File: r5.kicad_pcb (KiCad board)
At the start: 2 copper layers, 94.4 x 92.2 mm, 80 parts, among them J1 Conn_01x04, SW1 SW_SPDT, SW2 SW_SPDT, SW3 SW_SPDT, SW4 SW_SPDT, U1 LMZ22005, U10 74368PW, U100 Pico, U2 74LS365, U20 DRV8871DDA, U3 GY-BNO08X, U30 DRV8871DDA, U4 PI22, U40 DRV8871DDA, U5 SDD1309, U50 DRV8871DDA, U6 3X3HEADER, U60 DRV8871DDA, U70 DRV8871DDA, U80 PCA9685PW, X1 Conn_01x02, X2 Conn_01x02, X20 Conn_01x06, X30 Conn_01x06, X40 Conn_01x06, X50 Conn_01x06, X60 Conn_01x06, X70 Conn_01x06, X81 4X3HEADER

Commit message: wip
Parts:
- C90: moved to F.Cu
- D91: footprint LED_SMD:LED_WS2812B_PLCC4_5.0x5.0mm_P3.2mm -> LED_SMD:LED_WS2812B-2020_PLCC4_2.0x2.0mm; moved to F.Cu
- moved SW1 15.7 mm to (109.7, 137.4), turned to 90 degrees
- moved C90 14.0 mm to (97.0, 144.9), turned to 0 degrees
- moved D91 10.1 mm to (93.2, 144.8), turned to 180 degrees

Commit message: wip
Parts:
- removed C1: 10u, Capacitor_SMD:C_1206_3216Metric_Pad1.33x1.80mm_HandSolder
- removed U10: 74368PW, Package_SO:TSSOP-16_4.4x5mm_P0.65mm
- added J2: Conn_01x02, Connector_JST:JST_PH_B2B-PH-K_1x02_P2.00mm_Vertical, B.Cu at (86.7, 68.1)
- added R18: 300R, Resistor_SMD:R_0805_2012Metric, F.Cu at (116.1, 116.4)
- added U7: 74HC540, Package_SO:TSSOP-20_4.4x6.5mm_P0.65mm, F.Cu at (105.4, 82.5)
- C10, C20, C30, C4, C40, C50, C60, C70, C90: footprint Capacitor_SMD:C_0805_2012Metric_Pad1.18x1.45mm_HandSolder -> Capacitor_SMD:C_0805_2012Metric
- C2: value 10u -> 22u; footprint Capacitor_SMD:C_1206_3216Metric_Pad1.33x1.80mm_HandSolder -> Capacitor_SMD:C_1206_3216Metric
- C21, C31, C41, C51, C61, C71: value CP -> 22u; footprint Capacitor_SMD:CP_Elec_5x5.7 -> Capacitor_SMD:C_1206_3216Metric
- C80: value 10u -> 100n; footprint Capacitor_SMD:C_0805_2012Metric_Pad1.18x1.45mm_HandSolder -> Capacitor_SMD:C_0805_2012Metric
- C81: value CP -> 220u; footprint Capacitor_THT:CP_Radial_D6.3mm_P2.50mm -> Capacitor_SMD:CP_Elec_6.3x7.7
- D90: value DIODE-SOD523 -> 1N4148; footprint Diode_SMD:D_SOD-523 -> Diode_SMD:D_SOD-323
- D91: footprint LED_SMD:LED_WS2812B-2020_PLCC4_2.0x2.0mm -> LED_SMD:LED_WS2812B_PLCC4_5.0x5.0mm_P3.2mm
- R1, R10, R11, R12, R13, R14, R15, R16, R17, R3, R7, R8, R9: footprint Resistor_SMD:R_0805_2012Metric_Pad1.20x1.40mm_HandSolder -> Resistor_SMD:R_0805_2012Metric
- R2: value 1k3 -> 1k; footprint Resistor_SMD:R_0805_2012Metric_Pad1.20x1.40mm_HandSolder -> Resistor_SMD:R_0805_2012Metric
- R20, R30, R4, R40, R50, R60, R70: value 33k -> 68k; footprint Resistor_SMD:R_0805_2012Metric_Pad1.20x1.40mm_HandSolder -> Resistor_SMD:R_0805_2012Metric
- R5, R6: value dnc -> ~; footprint Resistor_SMD:R_0805_2012Metric_Pad1.20x1.40mm_HandSolder -> Resistor_SMD:R_0805_2012Metric
- R90, R91: value 1k8 -> 4k7; footprint Resistor_SMD:R_0805_2012Metric_Pad1.20x1.40mm_HandSolder -> Resistor_SMD:R_0805_2012Metric
- U2: value 74LS365 -> 74HC365
- moved C90 88.2 mm to (104.8, 57.1), turned to 180 degrees
- moved D91 84.6 mm to (105.9, 61.1)
- moved X2 81.0 mm to (97.9, 144.8)
- moved R17 54.1 mm to (102.1, 70.5), turned to 90 degrees
- moved R16 50.2 mm to (99.8, 70.9), turned to 90 degrees
- moved R15 46.8 mm to (97.7, 70.8), turned to 90 degrees
- moved R90 40.4 mm to (70.6, 57.7)
- moved R91 36.3 mm to (68.8, 60.5), turned to 90 degrees
- moved X20 35.4 mm to (150.8, 83.6), turned to 180 degrees
- moved X70 33.7 mm to (150.8, 116.4), turned to 180 degrees
- moved R14 30.9 mm to (122.2, 81.9), turned to 90 degrees
- moved X30 23.0 mm to (150.8, 90.2), turned to 180 degrees
- moved X60 21.4 mm to (150.8, 109.8), turned to 180 degrees
- moved R10 15.9 mm to (118.4, 116.1)
- moved R3 12.9 mm to (119.4, 112.4)
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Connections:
- C21 pad 2: GND -> GNDPWR
- C31 pad 2: GND -> GNDPWR
- C41 pad 2: GND -> GNDPWR
- C51 pad 2: GND -> GNDPWR
- C61 pad 2: GND -> GNDPWR
- C71 pad 2: GND -> GNDPWR
- R2 pad 2: GND -> Net-(R18-Pad1)
- U20 pad 7: GND -> GNDPWR
- U30 pad 7: GND -> GNDPWR
- U40 pad 7: GND -> GNDPWR
- U50 pad 7: GND -> GNDPWR
- U60 pad 7: GND -> GNDPWR
- U70 pad 7: GND -> GNDPWR
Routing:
- net GND: track 11.7 -> 0.00 mm, vias 16 -> 0
- net +BATT: track 2.40 -> 0.00 mm
- net VBATMEASURE: track 2.00 -> 0.00 mm
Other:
- copper layers 2 -> 4

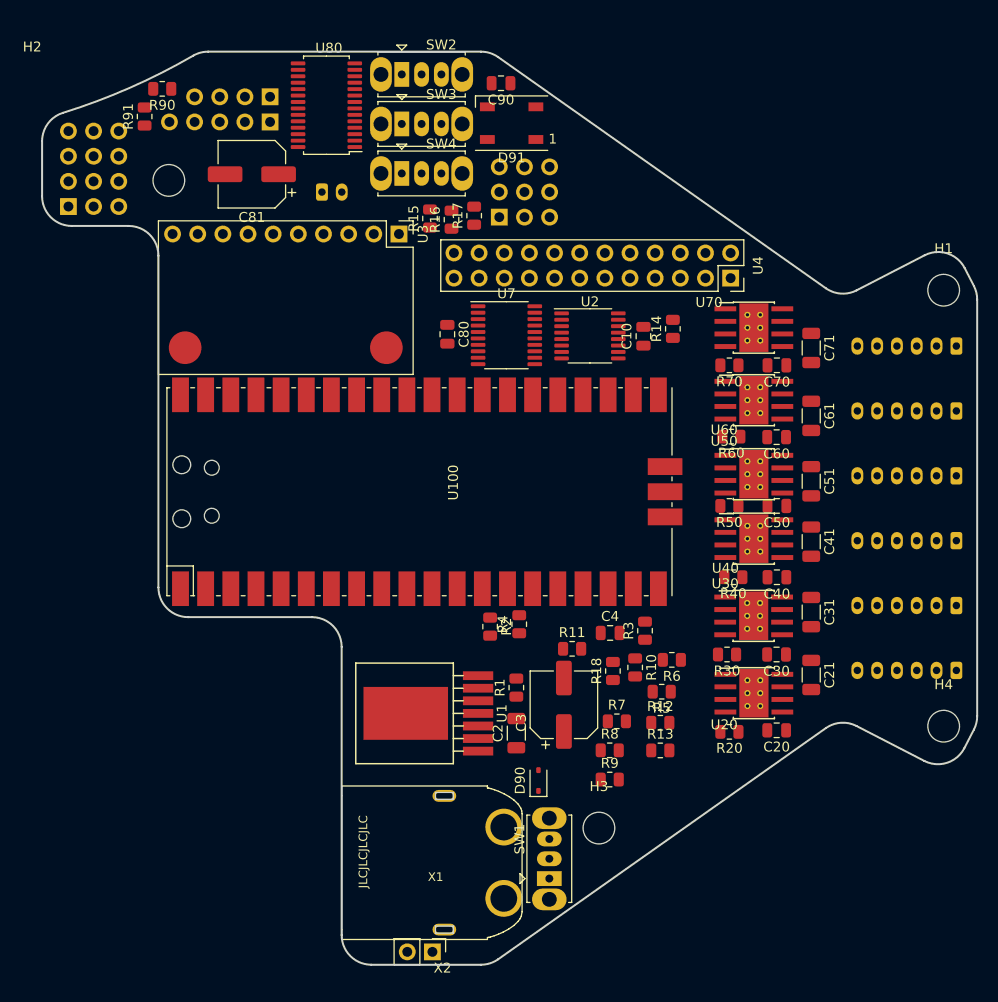
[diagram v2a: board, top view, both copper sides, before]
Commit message: component placement
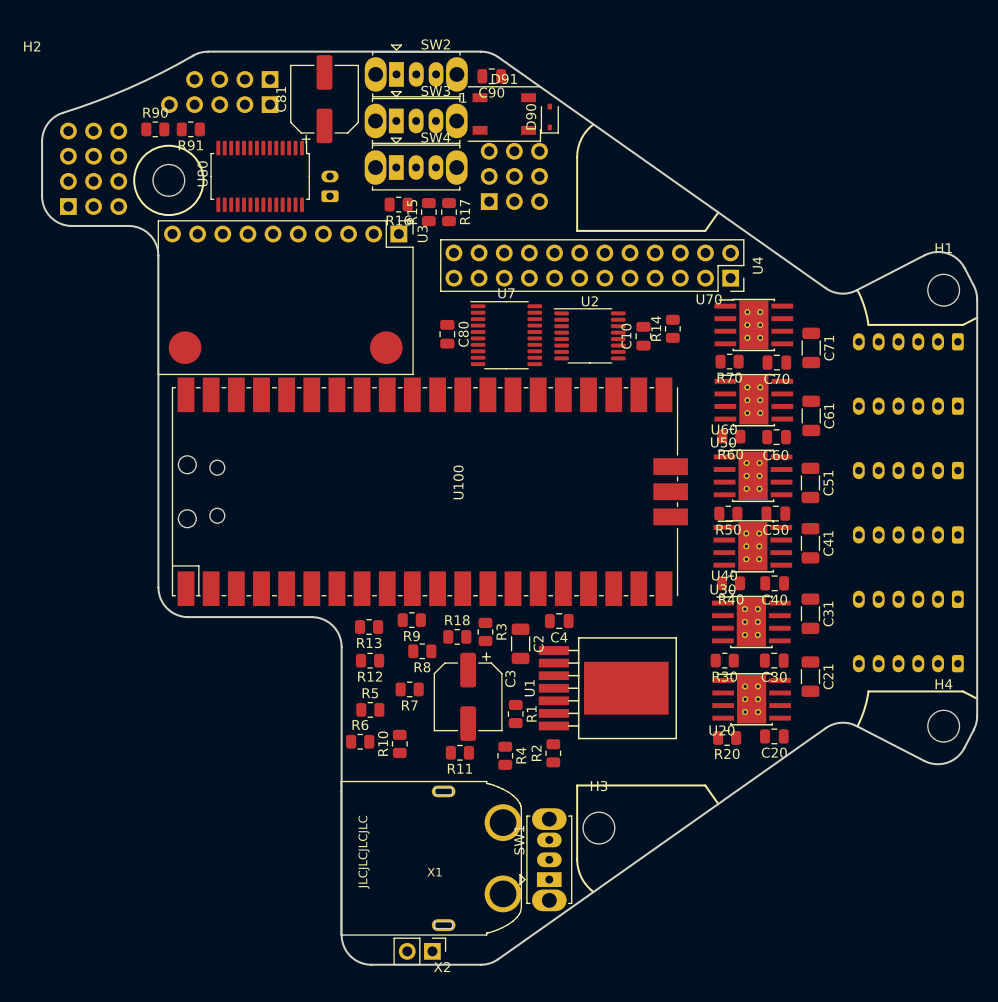
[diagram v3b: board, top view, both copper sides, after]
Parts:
- moved D90 67.0 mm to (109.8, 60.5)
- moved R6 32.5 mm to (90.6, 123.6), turned to 0 degrees
- moved R13 31.9 mm to (91.5, 112.0), turned to 180 degrees
- moved R12 30.0 mm to (91.6, 115.4), turned to 180 degrees
- moved R5 29.5 mm to (91.6, 120.4), turned to 0 degrees
- moved R9 25.7 mm to (95.8, 111.3), turned to 180 degrees
- moved R10 25.0 mm to (94.6, 123.8), turned to 90 degrees
- moved R8 21.4 mm to (96.9, 114.5), turned to 180 degrees
- moved R7 21.2 mm to (95.6, 118.3), turned to 180 degrees
- moved R3 16.1 mm to (103.2, 112.5), turned to -90 degrees
- moved R18 16.1 mm to (100.4, 113.0), turned to 0 degrees
- moved R11 15.4 mm to (100.7, 124.7), turned to 180 degrees
- moved R2 14.3 mm to (110.1, 124.8), turned to 90 degrees
- moved R4 13.4 mm to (105.2, 125.0), turned to -90 degrees
- moved C81 10.6 mm to (87.0, 58.7), turned to 90 degrees
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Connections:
- U100 pad 4: E6B -> E6A
- U100 pad 5: E6A -> E6B

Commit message: positions
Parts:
- removed the R17 at (99.6, 70.1)
- moved R40 55.2 mm to (70.8, 61.6), turned to 180 degrees
- moved R62 54.9 mm to (88.5, 68.7), turned to -90 degrees
- moved R61 51.6 mm to (90.5, 68.8), turned to -90 degrees
- moved R70 48.6 mm to (119.8, 82.2)
- moved R90 48.5 mm to (101.2, 70.1), turned to -90 degrees
- moved R92 48.3 mm to (111.2, 65.5), turned to -90 degrees
- moved R91 47.8 mm to (111.2, 68.9), turned to -90 degrees
- moved C28 38.0 mm to (132.5, 123.3)
- moved U25 38.0 mm to (130.1, 119.5)
- moved R25 38.0 mm to (127.7, 123.2), turned to 0 degrees
- moved C20 37.9 mm to (132.8, 85.2)
- moved R20 37.9 mm to (128.0, 85.3), turned to 0 degrees
- moved U20 37.9 mm to (130.5, 81.4)
- moved C23 33.5 mm to (137.0, 83.5)
- moved C31 32.4 mm to (137.1, 116.2)
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- renumbered C2 to C10, C3 to C11, C30 to C21, C40 to C22, C21 to C23, C31 to C24, C41 to C25, C50 to C26, C60 to C27, C70 to C28, C51 to C29, C61 to C30, C71 to C31, C90 to C40, C80 to C60, C4 to C70, C10 to C71, C81 to C90, D90 to D40, D91 to D41, H1 to H201, H2 to H202, H3 to H203, H4 to H204, R11 to R10, R12 to R11, R13 to R12, R1 to R13, R2 to R14, R18 to R15, R3 to R16, R4 to R17, R30 to R21, R40 to R22, R50 to R23, R60 to R24, R70 to R25, R14 to R40, R15 to R60, R5 to R61, R6 to R62, R10 to R70, R16 to R80, R7 to R90, R8 to R91, R9 to R92, R90 to R93, R91 to R94, SW1 to SW10, SW4 to SW60, SW2 to SW70, SW3 to SW80, U1 to U10, U30 to U21, U40 to U22, U50 to U23, U60 to U24, U70 to U25, U4 to U50, U80 to U60, U2 to U70, U7 to U71, U100 to U80, X1 to X10, X2 to X11, J2 to X12, X30 to X21, X40 to X22, X50 to X23, X60 to X24, X70 to X25, J1 to X40, U6 to X90, X81 to X91, U5 to X92, U3 to X93

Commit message: start routing
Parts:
- removed U70: 74HC365, Package_SO:TSSOP-16_4.4x5mm_P0.65mm
- added U51: 74HC541, Package_SO:TSSOP-20_4.4x6.5mm_P0.65mm, F.Cu at (106.1, 82.5)
- moved R70 18.4 mm to (101.6, 84.6), turned to -90 degrees
- moved C70 11.9 mm to (110.7, 80.5)
- moved U71 9.11 mm to (114.5, 82.5), turned to 90 degrees
- moved U24 3.55 mm to (133.6, 111.9)
- moved C27 3.55 mm to (135.8, 115.7)
- moved C22 3.55 mm to (135.9, 100.4)
- moved R23 3.43 mm to (131.1, 108.1)
- moved U23 3.43 mm to (133.6, 104.3)
- moved C26 3.43 mm to (135.8, 108.1)
- moved C20 3.39 mm to (136.2, 85.2)
- moved R21 3.38 mm to (131.1, 92.7)
- moved R24 3.36 mm to (131.1, 115.6)
- moved U22 3.36 mm to (133.6, 96.6)
- moved C21 3.27 mm to (135.9, 92.8)
- moved U20 3.24 mm to (133.7, 81.4)
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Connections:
- U71 pad 14: IM5 -> IM2
- U71 pad 15: IM6 -> IM3
- U71 pad 17: IM3 -> IM5
- U71 pad 18: IM2 -> IM6
- U71 pad 2: M2 -> M6
- U71 pad 3: M3 -> M5
- U71 pad 5: M6 -> M3
- U71 pad 6: M5 -> M2
- U80 pad 10: E5B -> E2B
- U80 pad 11: E4A -> E3A
- U80 pad 12: E4B -> E3B
- U80 pad 14: E1A -> E4A
- U80 pad 15: E1B -> E4B
- U80 pad 16: E2A -> E5A
- U80 pad 17: E2B -> E5B
- U80 pad 19: E3A -> E6A
- U80 pad 20: E3B -> E6B
- U80 pad 21: M6 -> M4
- U80 pad 24: M4 -> M6
- U80 pad 26: MENABLE -> M2
- U80 pad 27: M2 -> M1
- U80 pad 29: M1 -> MENABLE
- U80 pad 4: E6A -> ZERO0
- U80 pad 5: E6B -> WSLED
- U80 pad 6: ZERO0 -> E1A
- U80 pad 7: WSLED -> E1B
- U80 pad 9: E5A -> E2A
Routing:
- net GNDPWR: track 0.00 -> 94.0 mm
- net +BATT: track 0.00 -> 80.7 mm
- net E1B: track 0.00 -> 78.1 mm, vias 0 -> 1
- net E1A: track 0.00 -> 77.7 mm, vias 0 -> 1
- net E2A: track 0.00 -> 66.0 mm, vias 0 -> 1
- net E2B: track 0.00 -> 64.7 mm, vias 0 -> 1
- net E3A: track 0.00 -> 58.7 mm, vias 0 -> 1
- net E3B: track 0.00 -> 58.1 mm, vias 0 -> 1
- net E4A: track 0.00 -> 51.4 mm, vias 0 -> 1
- net IM6: track 0.00 -> 50.9 mm
- net E4B: track 0.00 -> 49.7 mm, vias 0 -> 1
- net EM5: track 0.00 -> 48.4 mm, vias 0 -> 2
- net EM4: track 0.00 -> 46.3 mm, vias 0 -> 2
- net EM6: track 0.00 -> 44.3 mm
- net IM5: track 0.00 -> 44.3 mm
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
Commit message: use 2 inverters
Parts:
- removed U51: 74HC541, Package_SO:TSSOP-20_4.4x6.5mm_P0.65mm
- added U70: 74HC540, Package_SO:TSSOP-20_4.4x6.5mm_P0.65mm, F.Cu at (118.7, 82.4)
- moved U71 4.98 mm to (109.5, 82.6)
- moved C70 3.40 mm to (114.1, 80.4), turned to 90 degrees
- moved C71 3.30 mm to (104.9, 80.4), turned to 90 degrees
- moved R70 3.30 mm to (104.9, 84.7)
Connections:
- U71 pad 13: IM1 -> IM4
- U71 pad 14: IM2 -> EM4
- U71 pad 15: IM3 -> IM5
- U71 pad 16: IM4 -> EM5
- U71 pad 17: IM5 -> IM6
- U71 pad 18: IM6 -> EM6
- U71 pad 2: M6 -> IM6
- U71 pad 3: M5 -> M6
- U71 pad 4: M4 -> IM5
- U71 pad 5: M3 -> M5
- U71 pad 6: M2 -> IM4
- U71 pad 7: M1 -> M4
- U80 pad 21: M4 -> M1
- U80 pad 22: M5 -> M2
- U80 pad 24: M6 -> M3
- U80 pad 25: M3 -> M4
- U80 pad 26: M2 -> M5
- U80 pad 27: M1 -> M6
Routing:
- net Net-(SW70-C): track 0.00 -> 25.8 mm, vias 0 -> 2
- net EM1: track 31.3 -> 13.1 mm, vias 2 -> 0
- net M1: track 21.9 -> 7.01 mm
- net EM2: track 34.8 -> 21.3 mm, vias 2 -> 0
- net EM6: track 44.3 -> 56.6 mm
- net IM6: track 50.9 -> 63.0 mm, vias 0 -> 2
- net EM3: track 38.2 -> 26.7 mm, vias 2 -> 0
- net M3: track 16.0 -> 6.50 mm
- net IM5: track 44.3 -> 52.6 mm, vias 0 -> 2
- net +3.3V: track 0.00 -> 7.41 mm
- net IM2: track 20.5 -> 27.7 mm, vias 0 -> 2
- net M2: track 13.9 -> 6.78 mm
- net IM4: track 37.2 -> 44.0 mm, vias 0 -> 2
- net IM1: track 15.6 -> 21.5 mm, vias 0 -> 2
- net M5: track 10.0 -> 4.31 mm
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
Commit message: routing
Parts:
- moved U22 2.85 mm to (130.7, 96.6)
- moved U25 1.22 mm to (130.6, 119.3)
- moved C27 0.65 mm to (136.5, 115.6)
- moved U71 0.20 mm to (109.5, 82.4)
- moved C70 0.10 mm to (114.1, 80.3)
- moved C71 0.10 mm to (104.9, 80.3)
- moved R70 0.10 mm to (104.9, 84.6)
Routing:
- net IM6: track 63.0 -> 59.7 mm
- net IM3: track 31.4 -> 29.2 mm
- net EM3: track 26.7 -> 25.0 mm
- net Net-(SW70-C): track 25.8 -> 26.8 mm
- net IM2: track 27.7 -> 26.6 mm
- net EM2: track 21.3 -> 20.3 mm
- net EM5: track 49.1 -> 48.5 mm

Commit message: routing continued
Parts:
- added NT50: NetTie_2, NetTie:NetTie-2_SMD_Pad2.0mm, F.Cu at (103.3, 126.2)
- moved R40 10.9 mm to (81.7, 61.2), turned to 0 degrees
- moved C30 3.61 mm to (136.3, 112.4)
- moved C27 3.30 mm to (133.2, 115.5)
- moved U20 3.00 mm to (130.7, 81.3)
- moved R20 3.00 mm to (128.2, 85.1)
- moved C20 2.95 mm to (133.2, 85.1)
- moved U21 2.90 mm to (130.7, 88.9)
- moved R23 2.86 mm to (128.2, 107.9)
- moved U23 2.86 mm to (130.7, 104.1)
- moved U24 2.85 mm to (130.7, 111.7)
- moved R24 2.85 mm to (128.2, 115.5)
- moved R21 2.85 mm to (128.2, 92.7)
- moved R22 2.85 mm to (128.2, 100.3)
- moved C23 2.80 mm to (136.3, 82.0)
- moved C21 2.75 mm to (133.2, 92.7)
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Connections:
- U60 pad 12: unconnected-(U60-LED6-Pad12) -> S2
- U60 pad 13: unconnected-(U60-LED7-Pad13) -> S1
- U60 pad 15: unconnected-(U60-LED8-Pad15) -> S3
- U60 pad 16: unconnected-(U60-LED9-Pad16) -> S4
- U60 pad 6: S1 -> unconnected-(U60-LED0-Pad6)
- U60 pad 7: S2 -> unconnected-(U60-LED1-Pad7)
- U60 pad 8: S3 -> unconnected-(U60-LED2-Pad8)
- U60 pad 9: S4 -> unconnected-(U60-LED3-Pad9)
- U80 pad 31: ZERO2 -> ZERO1
- U80 pad 32: ZERO1 -> ZERO2
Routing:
- net INBUTTON: track 0.00 -> 72.9 mm
- net IMURST: track 0.00 -> 57.7 mm
- net GNDPWR: track 94.0 -> 40.0 mm, vias 0 -> 21
- net OLEDRES: track 0.00 -> 51.3 mm
- net OLEDSDA: track 0.00 -> 46.9 mm
- net OLEDSCL: track 0.00 -> 42.5 mm
- net ZERO2: track 0.00 -> 34.6 mm
- net IMUPS1: track 0.00 -> 32.8 mm
- net ZERO1: track 0.00 -> 32.0 mm
- net IMUPS0: track 0.00 -> 30.3 mm
- net GND: track 2.63 -> 32.5 mm, vias 0 -> 12
- net +BATT: track 80.7 -> 53.0 mm, vias 0 -> 20
- net Net-(SW60-B): track 0.00 -> 23.6 mm
- net +3.3V: track 7.41 -> 25.9 mm
- net S4: track 0.00 -> 17.7 mm
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- added copper zone on In2.Cu, net +BATT
- added copper zone on F.Cu, net GND
- added copper zone on In1.Cu, net GND
- added copper zone on In1.Cu, net GNDPWR
